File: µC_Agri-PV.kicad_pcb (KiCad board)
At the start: 4 copper layers, 113 x 113 mm, 227 parts, among them IC1 ESDALC6V1W5, IC201 ESDALC6V1W5, IC202 ESDALC6V1W5, IC203 ESDALC6V1W5, IC601 MMS9013-L-TP, IC602 MMS9013-L-TP, IC701 TPS63021DSJR, IC8 317990687, J206 Conn_01x04_Pin, J207 Conn_01x07_Pin, J4 USB_B_Micro, J502 503398-1892, J6 Conn_Coaxial, J601 USB_B_Micro, Q201 DMG1012T-13, Q202 DMG1012T-13, Q203 DMG1012T-13, Q204 DMG1012T-13, Q501 IRLML6402, Q7 IRLML6402, Q8 IRLML6402, Q801 IRLML6402, Q802 IRLML6402, Q803 IRLML6402, Q804 IRLML6402, Q805 IRLML6402, SW2 SW_DIP_x01, SW3 SW_DIP_x01, U201 TLV9304IDR, U202 STM32U575ZIT6Q, U3 ESP32-C6-WROOM-1-N8, U4 AMS1117-3.3, U702 TLV9304IDR, U801 TPS61023DRLR, U802 ISL83078EIBZA, X601 XTAL_4_PINS, X602 XTAL_2_PINS

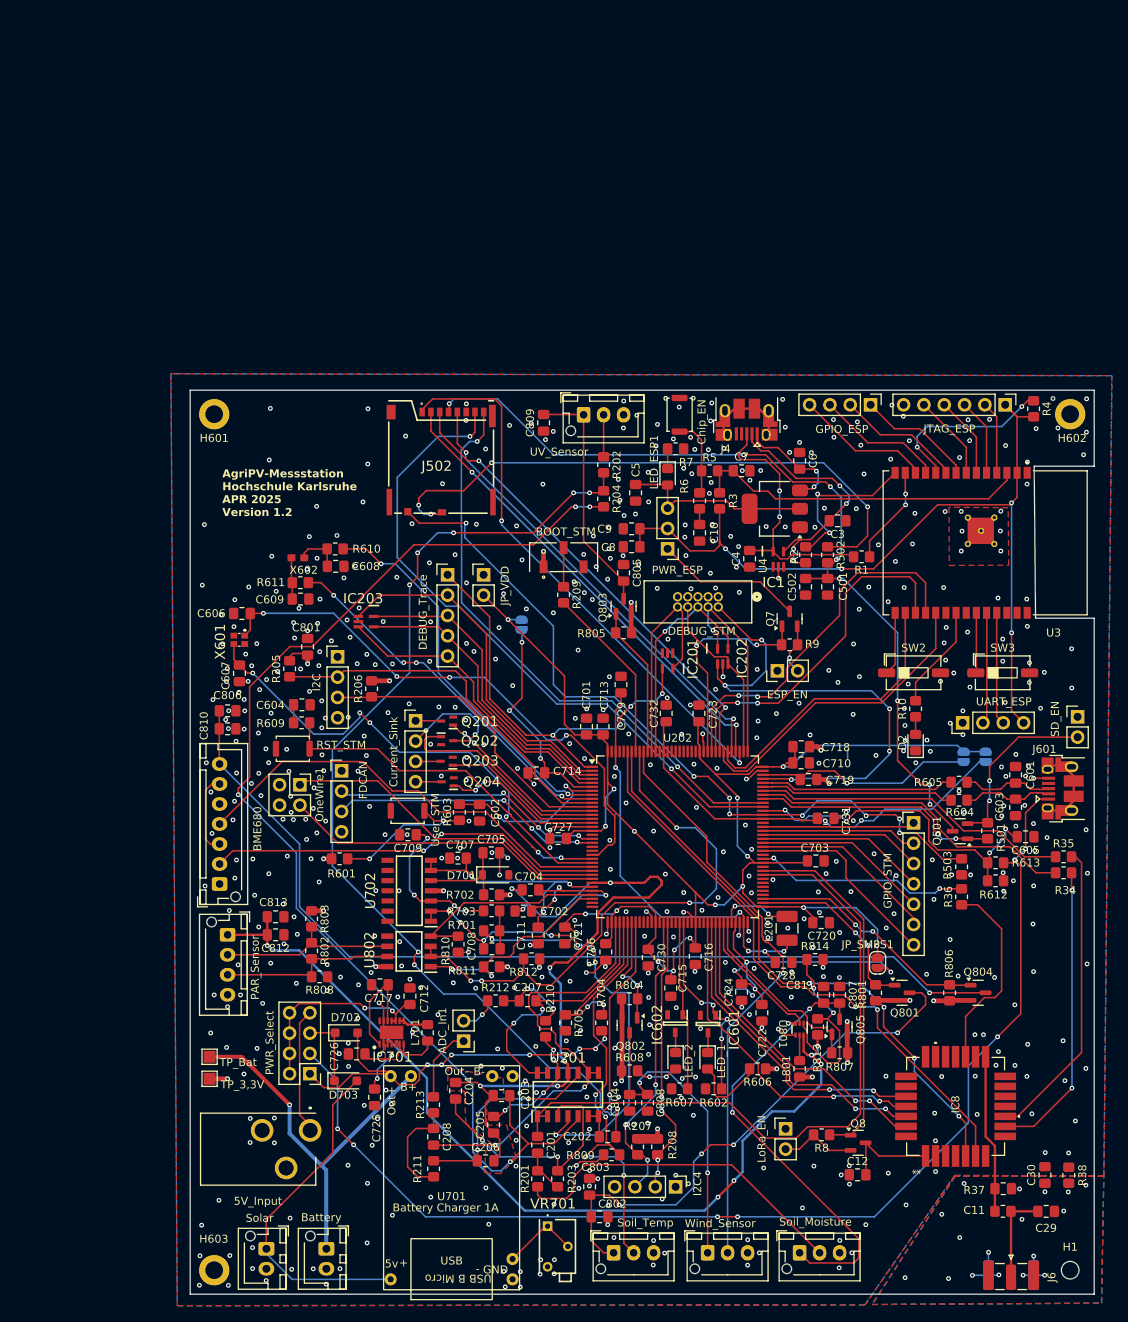
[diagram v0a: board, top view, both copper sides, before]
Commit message: Add TP4056-18650 footprint and update Power schematic
Added the TP4056-18650-2 footprint to the library and assigned it to the battery charger in Power.kicad_sch. Updated the Power schematic to improve symbol details, add descriptive properties, and enhance the 3V3 lane toggling section. Made various net and annotation adjustments, and removed obsolete autosave and lock files.
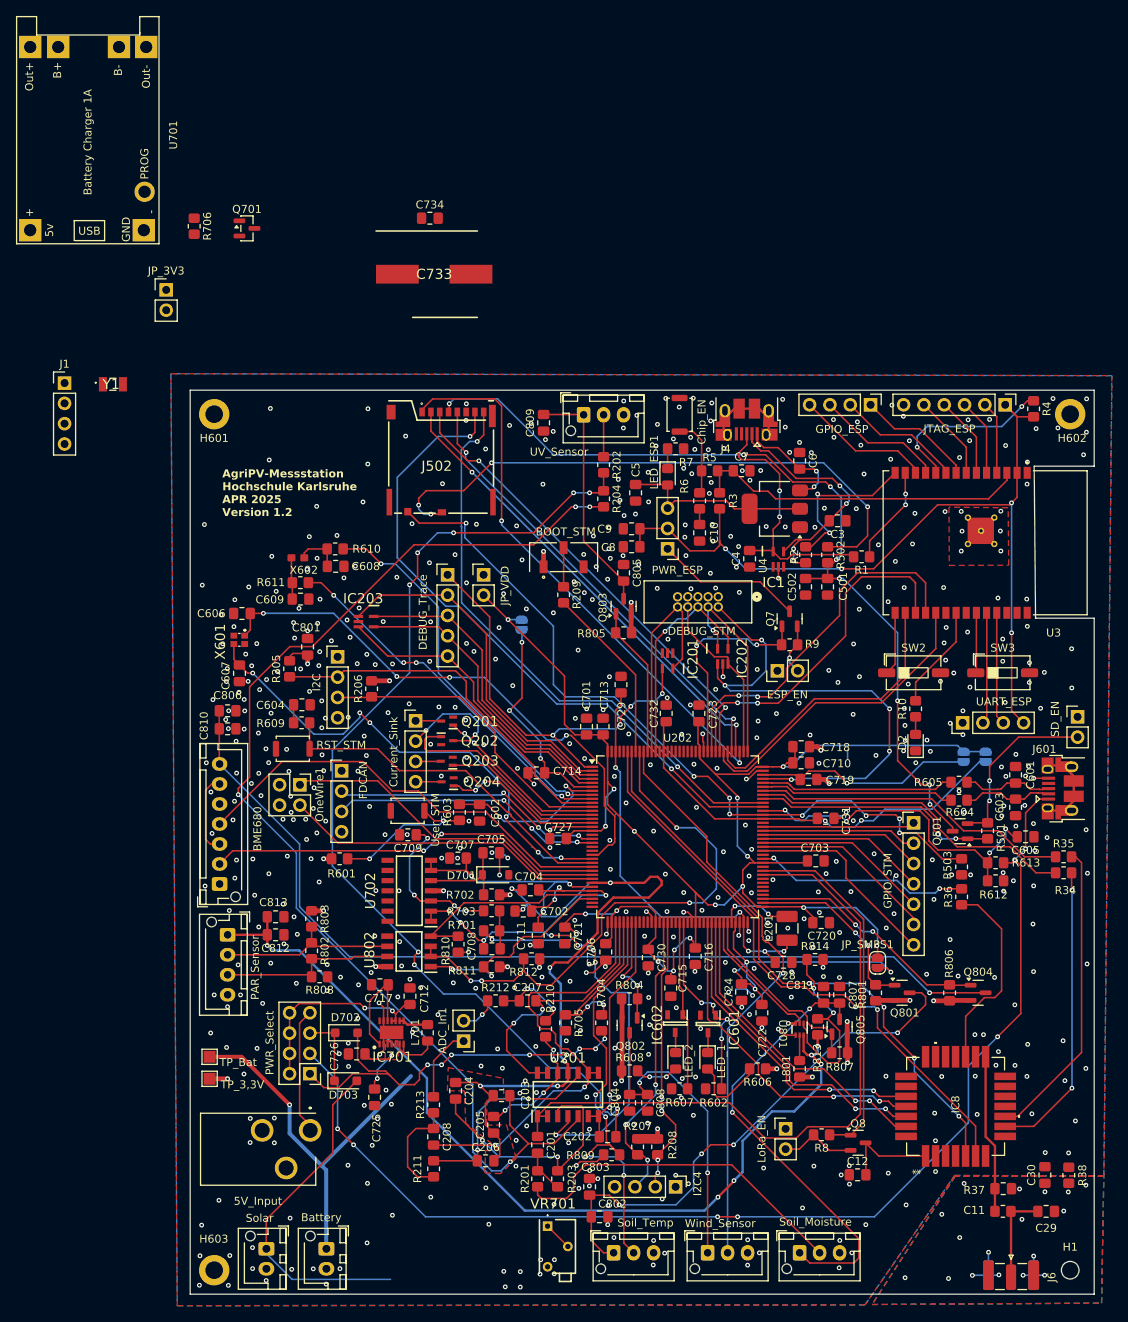
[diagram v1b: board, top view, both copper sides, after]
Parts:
- added C733: FC0V104ZFTBR24, SamacSys_Parts:CAPAE1080X550N, F.Cu at (48.0, 20.5)
- added C734: 100n, Capacitor_SMD:C_0805_2012Metric_Pad1.18x1.45mm_HandSolder, F.Cu at (47.5, 13.5)
- added J1: Conn_01x04_Pin, Connector_PinHeader_2.54mm:PinHeader_1x04_P2.54mm_Vertical, F.Cu at (1.79, 34.1)
- added JP_3V3: Jumper_2_Bridged, Connector_PinHeader_2.54mm:PinHeader_1x02_P2.54mm_Vertical, F.Cu at (14.5, 22.5)
- added Q701: IRLML6402, Package_TO_SOT_SMD:SOT-23, F.Cu at (24.6, 14.8)
- added R706: 100k, Resistor_SMD:R_0805_2012Metric_Pad1.20x1.40mm_HandSolder, F.Cu at (18.0, 14.5)
- added Y1: FC-13532.7680KA-AG5, SamacSys_Parts:FC135327680KAAG5, F.Cu at (7.84, 34.3)
- U701: footprint TP4056:TP4056-18650 -> TP4056:TP4056-18650-2
- moved U701 128.8 mm to (-4.20, 16.7), turned to 90 degrees
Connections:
- C701 pad 1: /Power Supply/Vdd_MCU -> VBAT
- C703 pad 1: /Power Supply/Vdd_MCU -> VBAT
- C706 pad 1: /Power Supply/Vdd_MCU -> VBAT
- C710 pad 1: /Power Supply/Vdd_MCU -> VBAT
- C713 pad 1: /Power Supply/Vdd_MCU -> VBAT
- C715 pad 1: /Power Supply/Vdd_MCU -> VBAT
- C716 pad 1: /Power Supply/Vdd_MCU -> VBAT
- C718 pad 1: /Power Supply/Vdd_MCU -> VBAT
- C720 pad 1: /Power Supply/Vdd_MCU -> VBAT
- C721 pad 1: /Power Supply/Vdd_MCU -> VBAT
- C723 pad 1: /Power Supply/Vdd_MCU -> VBAT
- C725 pad 1: +3.3V -> /Power Supply/3V3_VDD
- C726 pad 1: +3.3V -> /Power Supply/3V3_VDD
- C727 pad 1: /Power Supply/Vdd_MCU -> VBAT
- C730 pad 1: /Power Supply/Vdd_MCU -> VBAT
- DEBUG1 pad 10: /STM32U575ZIT6Q/DEBUG_JTRST -> /IO and mounting holes/DEBUG_NRST
- IC201 pad 5: /STM32U575ZIT6Q/DEBUG_JTRST -> /IO and mounting holes/DEBUG_NRST
- IC701 pad 3: +3.3V -> /Power Supply/3V3_VDD
- IC701 pad 4: +3.3V -> /Power Supply/3V3_VDD
- IC701 pad 5: +3.3V -> /Power Supply/3V3_VDD
- JP_IO2 pad 1: /Power Supply/Vdd_MCU -> VBAT
- JP_SMPS1 pad 1: /Power Supply/Vdd_MCU -> VBAT
- JP_USB1 pad 1: /Power Supply/Vdd_MCU -> VBAT
- JP_VDD1 pad 1: +3.3V -> /Power Supply/3V3_VDD
- JP_VDD1 pad 2: /Power Supply/Vdd_MCU -> VBAT
- R609 pad 2: /IO and mounting holes/NRST -> /IO and mounting holes/DEBUG_NRST
- R701 pad 1: /Power Supply/Vdd_MCU -> VBAT
- Reset1 pad 2: /IO and mounting holes/NRST -> /IO and mounting holes/DEBUG_NRST
- TP_3,3V1 pad 1: +3.3V -> /Power Supply/3V3_VDD
- U202 pad 108: /Power Supply/Vdd_MCU -> VBAT
- U202 pad 121: /Power Supply/Vdd_MCU -> VBAT
- U202 pad 133: /STM32U575ZIT6Q/DEBUG_JTRST -> unconnected-(U202-PB4-Pad133)
- U202 pad 144: /Power Supply/Vdd_MCU -> VBAT
- U202 pad 17: /Power Supply/Vdd_MCU -> VBAT
- U202 pad 25: /IO and mounting holes/NRST -> /IO and mounting holes/DEBUG_NRST
- U202 pad 35: unconnected-(U202-PA2-Pad35) -> Net-(J1-Pin_2)
- U202 pad 36: unconnected-(U202-PA3-Pad36) -> Net-(J1-Pin_3)
- U202 pad 38: /Power Supply/Vdd_MCU -> VBAT
- U202 pad 49: /Power Supply/Vdd_MCU -> VBAT
- U202 pad 59: /Power Supply/Vdd_MCU -> VBAT
- U202 pad 73: /Power Supply/Vdd_MCU -> VBAT
- U202 pad 76: unconnected-(U202-PB15-Pad76) -> /Power Supply/3V3_EN
- U202 pad 84: /Power Supply/Vdd_MCU -> VBAT
- U701 pad 1: GND -> Net-(D703-A)
- U701 pad 2: Net-(U701-R_trim) -> GND
- U701 pad 3: GND -> /Power Supply/Vdd_Bat
- U701 pad 6: /Power Supply/Vdd_Bat -> GND
- U701 pad 7: Net-(D703-A) -> Net-(U701-PROG)
- VR701 pad 1: Net-(U701-R_trim) -> Net-(U701-PROG)
- VR701 pad 2: Net-(U701-R_trim) -> Net-(U701-PROG)
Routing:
- net /IO and mounting holes/NRST: track 44.6 -> 0.00 mm
- net /IO and mounting holes/DEBUG_NRST: track 0.00 -> 44.6 mm
- net /STM32U575ZIT6Q/DEBUG_JTRST: track 27.8 -> 0.00 mm
- net (no net): track 0.00 -> 27.8 mm
- net +3.3V: track 69.7 -> 58.6 mm, vias 25 -> 23
- net /Power Supply/3V3_VDD: track 0.00 -> 11.2 mm, vias 0 -> 2
- net Net-(U701-R_trim): track 9.67 -> 0.00 mm
- net Net-(U701-PROG): track 0.00 -> 3.86 mm

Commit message: Update schematic and PCB version to 1.3, update dates
Updated revision numbers and dates to 2025-12-18 (version 1.3) across all KiCad schematic files and the PCB. Adjusted the board text to reflect the new version and date. Also updated backup ZIP file and made a minor property fix in Power.kicad_sch.
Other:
- board text added: "AgriPV-Messstation Hochschule Karlsruhe DEZ 2025 Version 1.3"
- board text removed: "AgriPV-Messstation Hochschule Karlsruhe APR 2025 Version 1.2"
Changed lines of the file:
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@@
 		)
 	)
-	(gr_text "AgriPV-Messstation\nHochschule Karlsruhe\nAPR 2025 \nVersion 1.2 "
+	(gr_text "AgriPV-Messstation\nHochschule Karlsruhe\nDEZ 2025 \nVersion 1.3 "
 		(at 21.51 50.85 0)
 		(layer "F.SilkS")
